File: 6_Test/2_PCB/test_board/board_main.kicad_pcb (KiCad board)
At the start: 4 copper layers, 100.5 x 75 mm, 80 parts, among them J1 PWR_Supply_Pins, J10 Chip_AVSS_GND_Jumpers, J11 Buffer_PWR_Jumper, J12 Reset_PWR_Jumpers, J13 Reset_Signal_Jumpers, J2 Analog_Input_Pins, J3 Digital_Input_Pins, J4 Digital_Output_Pins, J5 Chip_VDD_Jumpers, J6 BNC_Odd, J7 BNC_Even, J8 BNC_Jumpers, J9 Analog_Input_Jumpers, U1 TPS74501PDRVR, U2 ADA4807-1AKSZ-R7, U3 ADA4807-1AKSZ-R7, U4 TPS74501PDRVR, U5 SN74HC74DR, U6 CD4001BM96, U7 SN74LVC245APWR, U8 SN74LVC245APWR

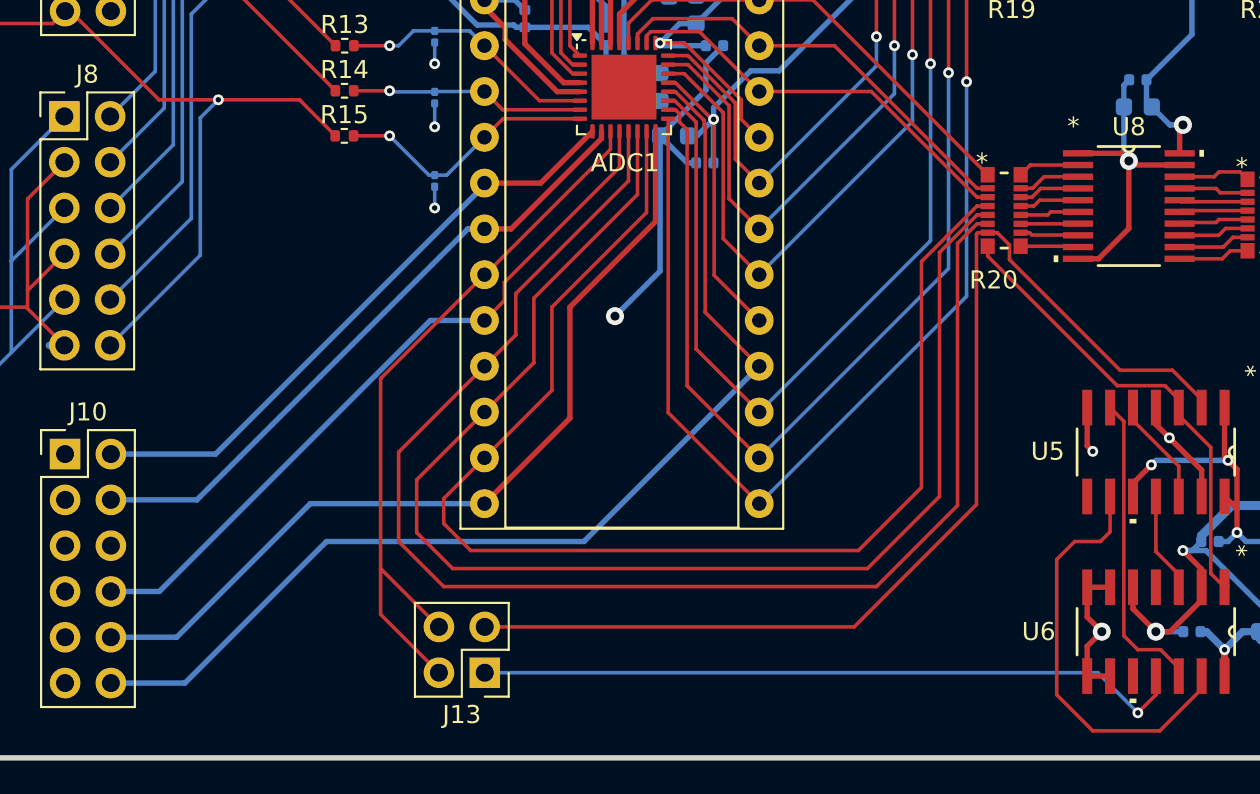
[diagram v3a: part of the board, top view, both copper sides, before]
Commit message: Fixed DRC errors
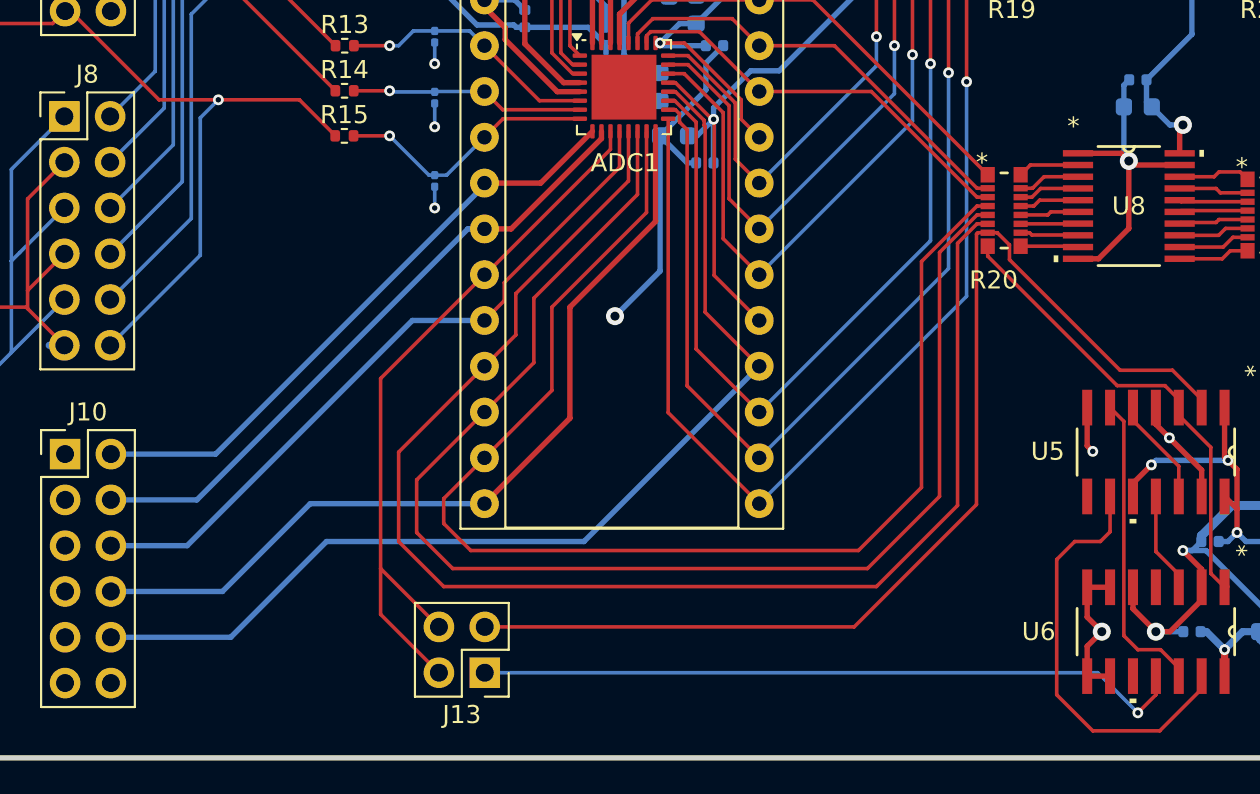
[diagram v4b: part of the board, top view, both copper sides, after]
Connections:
- J10 pad A3: /ADC/AVSS -> GND
- J10 pad B3: GND -> Net-(ADC1-IOVSS-Pad12)
- J10 pad B4: Net-(ADC1-IOVSS-Pad12) -> Net-(ADC1-VSS)
- J10 pad B5: Net-(ADC1-VSS) -> Net-(ADC1-IOVSS-Pad20)
- J10 pad B6: Net-(ADC1-IOVSS-Pad20) -> /ADC/AVSS
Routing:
- net Net-(ADC1-IOVSS-Pad12): track 40.5 -> 39.5 mm
- net Net-(ADC1-VSS): track 48.4 -> 47.3 mm
- net Net-(ADC1-IOVSS-Pad20): track 60.8 -> 59.7 mm
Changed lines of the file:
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@@
 		(tags "SN74LVC245APWR ")
 		(property "Reference" "U8"
-			(at 0 -4.3928 0)
+			(at 0 0 0)
 			(unlocked yes)
 			(layer "F.SilkS")
@@
 		(fp_text user "*"
 			(at -3.0734 -4.423601 0)
+			(unlocked yes)
+			(layer "F.SilkS")
+			(effects
+				(font
+					(size 1 1)
+					(thickness 0.15)
+				)
+			)
+		)
+		(fp_text user "*"
+			(at -3.0734 -4.423601 0)
 			(layer "F.SilkS")
 			(effects
@@
 		(fp_text user "*"
 			(at -3.0734 -4.423601 0)
+			(unlocked yes)
 			(layer "F.Fab")
 			(effects
@@
 		(fp_text user "*"
 			(at -3.0734 -4.423601 0)
-			(unlocked yes)
 			(layer "F.Fab")
 			(effects
@@
 			(pintype "power_in")
 		)
-		(model "${KIPRJMOD}/TestBoardEDA/SN74LVC245APWR.stp"
-			(offset
-				(xyz 0 0 0)
-			)
-			(scale
-				(xyz 1 1 1)
-			)
-			(rotate
-				(xyz 0 0 0)
-			)
-		)
 	)
 	(footprint "ECE628_lib:bnc_mini_gnd"
@@
 		)
 		(pad "A3" thru_hole oval
-			(at 2.54 5.08)
+			(at 0 5.08)
 			(size 1.7 1.7)
 			(drill 1)
 			(layers "*.Cu" "*.Mask")
 			(remove_unused_layers no)
-			(net 36 "/ADC/AVSS")
+			(net 34 "GND")
 			(pinfunction "A3")
 			(pintype "unspecified")
@@
 		)
 		(pad "B3" thru_hole oval
-			(at 0 5.08)
+			(at 2.54 5.08)
 			(size 1.7 1.7)
 			(drill 1)
 			(layers "*.Cu" "*.Mask")
 			(remove_unused_layers no)
-			(net 34 "GND")
+			(net 27 "Net-(ADC1-IOVSS-Pad12)")
 			(pinfunction "B3")
 			(pintype "unspecified")
@@
 			(layers "*.Cu" "*.Mask")
 			(remove_unused_layers no)
-			(net 27 "Net-(ADC1-IOVSS-Pad12)")
+			(net 6 "Net-(ADC1-VSS)")
 			(pinfunction "B4")
 			(pintype "unspecified")
@@
 			(layers "*.Cu" "*.Mask")
 			(remove_unused_layers no)
-			(net 6 "Net-(ADC1-VSS)")
+			(net 25 "Net-(ADC1-IOVSS-Pad20)")
 			(pinfunction "B5")
 			(pintype "unspecified")
@@
 			(layers "*.Cu" "*.Mask")
 			(remove_unused_layers no)
-			(net 25 "Net-(ADC1-IOVSS-Pad20)")
+			(net 36 "/ADC/AVSS")
 			(pinfunction "B6")
 			(pintype "unspecified")
@@
 	)
 	(segment
-		(start 97.19 132.81)
-		(end 93.54 132.81)
+		(start 93.54 130.27)
+		(end 99.73 130.27)
 		(width 0.3)
 		(layer "B.Cu")
@@
 	)
 	(segment
-		(start 104.6 125.4)
-		(end 97.19 132.81)
+		(start 99.73 130.27)
+		(end 104.6 125.4)
 		(width 0.3)
 		(layer "B.Cu")
@@
 	)
 	(segment
-		(start 93.54 135.35)
-		(end 97.65 135.35)
+		(start 100.19 132.81)
+		(end 93.54 132.81)
 		(width 0.3)
 		(layer "B.Cu")
@@
 	)
 	(segment
-		(start 119.78 127.5)
-		(end 129.5 117.78)
+		(start 105.5 127.5)
+		(end 100.19 132.81)
 		(width 0.3)
 		(layer "B.Cu")
@@
 	)
 	(segment
-		(start 97.65 135.35)
-		(end 105.5 127.5)
+		(start 119.78 127.5)
+		(end 129.5 117.78)
 		(width 0.3)
 		(layer "B.Cu")
@@
 	)
 	(segment
-		(start 93.54 130.27)
-		(end 96.23 130.27)
+		(start 93.54 127.73)
+		(end 97.77 127.73)
 		(width 0.3)
 		(layer "B.Cu")
@@
 	)
 	(segment
-		(start 111.26 115.24)
+		(start 110.26 115.24)
 		(end 114.26 115.24)
 		(width 0.3)
@@
 	)
 	(segment
-		(start 96.23 130.27)
-		(end 111.26 115.24)
+		(start 97.77 127.73)
+		(end 110.26 115.24)
 		(width 0.3)
 		(layer "B.Cu")

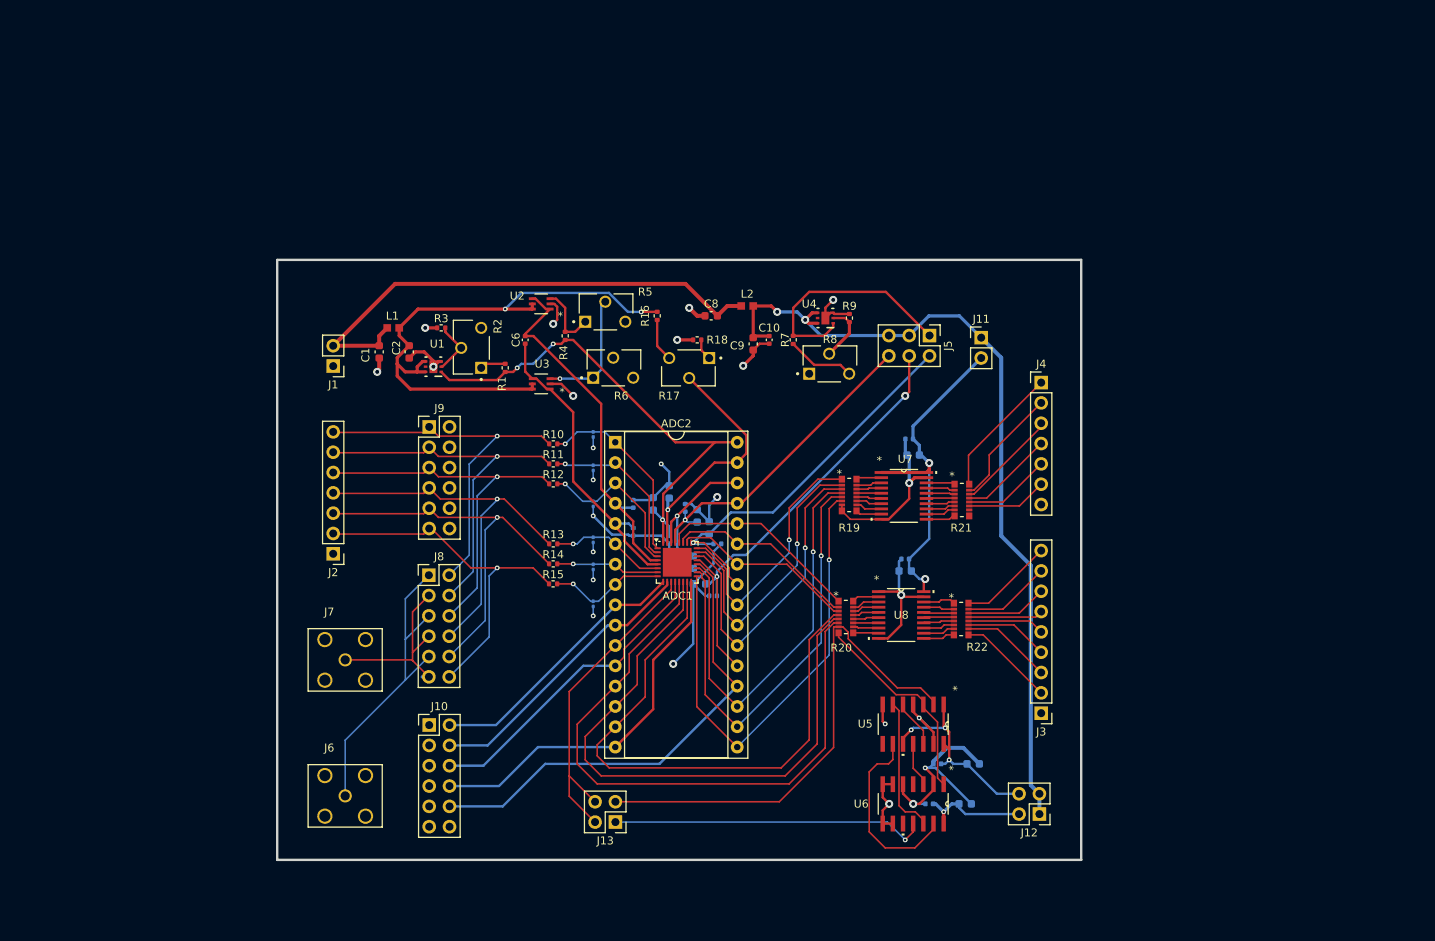
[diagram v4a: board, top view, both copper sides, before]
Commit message: Board Edits 250206
- Added the terminal block (4 positions - VSUP, GND, GND, & AVSS)
- Added vias for test points
- Added silkscreen labels for all inputs, jumpers, and potentiometers
- Widened traces going across the board
- Relabeled plane as AVSS plane
- Fixes to 3D model of board
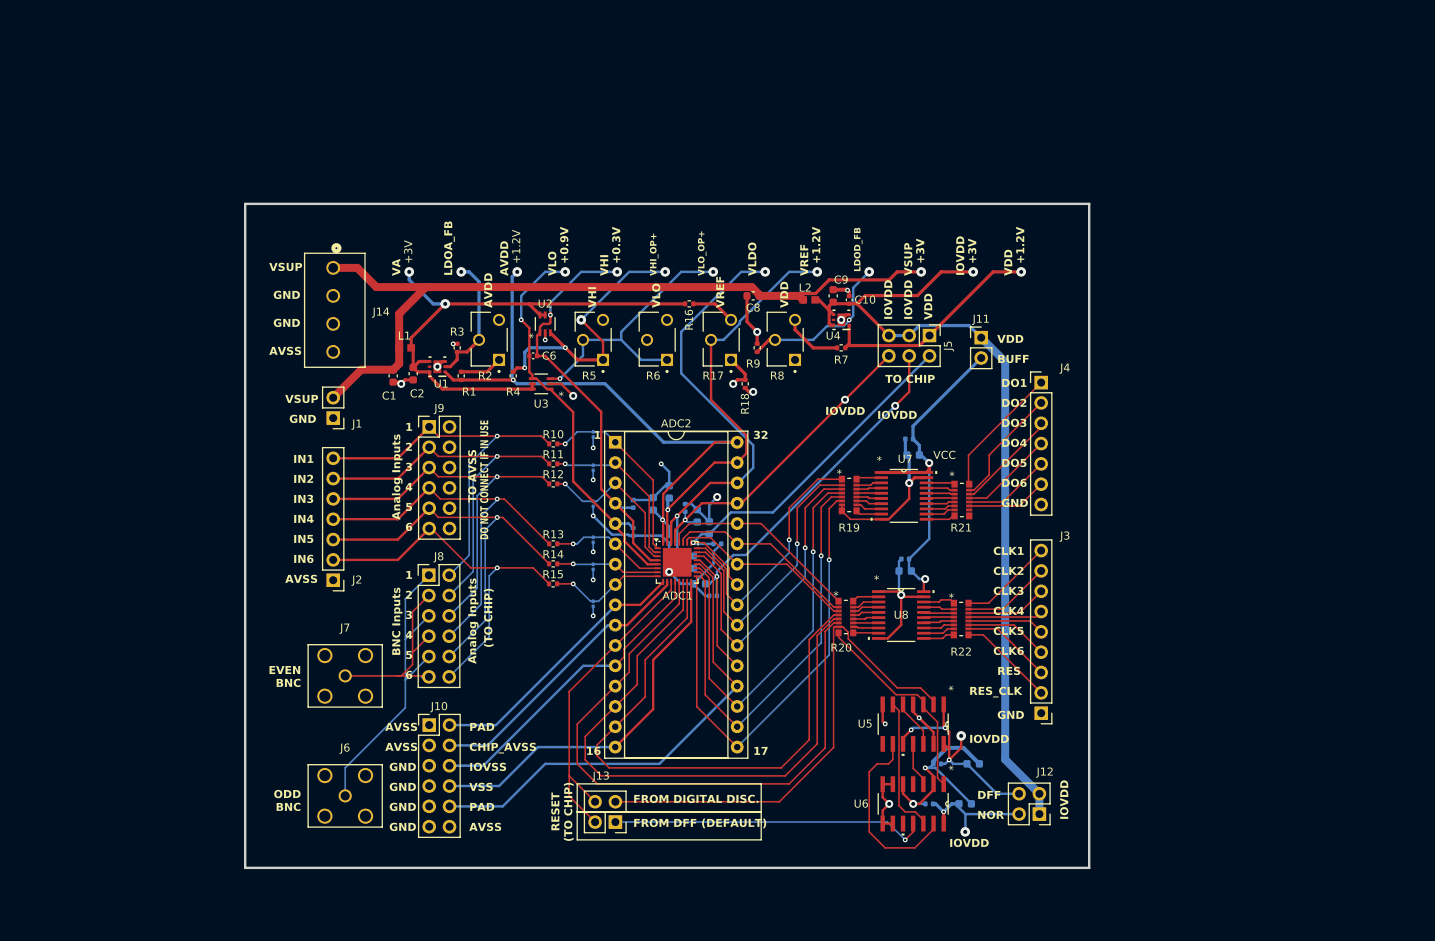
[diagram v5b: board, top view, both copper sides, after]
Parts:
- added J14: 1546551-4, TermBlck_4posFootprints:CONN4_1546551-4_TEC, F.Cu at (79.0, 65.5)
- moved R9 12.1 mm to (132.0, 75.5)
- moved C9 11.7 mm to (141.5, 69.0), turned to 90 degrees
- moved C10 11.2 mm to (143.5, 69.5), turned to 90 degrees
- moved R4 8.20 mm to (101.5, 79.0)
- moved R18 8.14 mm to (130.5, 80.0), turned to -90 degrees
- moved L2 7.79 mm to (138.5, 69.5)
- moved R6 6.52 mm to (119.5, 74.5), turned to 90 degrees
- moved J1 6.50 mm to (79.0, 84.3)
- moved R8 6.26 mm to (135.5, 74.5), turned to 90 degrees
- moved R7 6.08 mm to (142.5, 75.5), turned to 180 degrees
- moved C8 5.81 mm to (131.5, 69.0)
- moved R1 5.59 mm to (95.0, 79.0)
- moved R17 5.32 mm to (127.5, 74.5), turned to 90 degrees
- moved R16 4.27 mm to (123.5, 70.0), turned to 0 degrees
- moved R5 3.81 mm to (111.5, 74.5), turned to 90 degrees
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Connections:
- ADC1 pad 33: (no net) -> GND
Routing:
- net /ADC/VLDO: track 20.0 -> 57.1 mm, vias 1 -> 2
- net /AnalogSupply/VSUP: track 64.8 -> 98.4 mm, vias 0 -> 1
- net Net-(U2-+IN): track 8.39 -> 36.0 mm, vias 0 -> 4
- net /ADC/VREF: track 30.9 -> 51.5 mm, vias 1 -> 2
- net Net-(U3-+IN): track 15.6 -> 34.4 mm, vias 1 -> 2
- net GND: track 132.7 -> 117.8 mm
- net Net-(U4-FB): track 7.23 -> 20.3 mm, vias 0 -> 2
- net /ADC/VLO: track 38.2 -> 51.1 mm, vias 0 -> 2
- net /ADC/AVDD: track 64.1 -> 76.0 mm
- net Net-(U1-FB): track 6.80 -> 16.2 mm, vias 0 -> 1
- net /ADC/VHI: track 45.9 -> 53.1 mm, vias 0 -> 2
- net Net-(U5-*1CLR): track 34.2 -> 37.8 mm, vias 4 -> 5
- net /ADC/IN1: track 48.0 -> 50.4 mm
- net /ADC/IOVDD: track 104.4 -> 106.7 mm, vias 2 -> 1
- net Net-(R17-Pad1): track 2.68 -> 4.93 mm, vias 0 -> 1
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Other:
- board size 100.5 x 75 mm -> 105.5 x 83 mm
- board text added: "(TO CHIP)"
- board text added: "+0.3V"
- board text added: "+0.9V"
- board text added: "+1.2V"
- board text added: "+3V"
- board text added: "1"
- board text added: "16"
- board text added: "17"
- board text added: "2"
- board text added: "3"
- board text added: "32"
- board text added: "4"
- board text added: "5"
- board text added: "6"
- board text added: "AVDD"
- board text added: "AVSS"
- board text added: "Analog Inputs"
- board text added: "BNC Inputs"
- board text added: "BUFF"
- board text added: "CHIP_AVSS"
- board text added: "CLK1"
- board text added: "CLK2"
- board text added: "CLK3"
- board text added: "CLK4"
- board text added: "CLK5"
- board text added: "CLK6"
- board text added: "DFF"
- board text added: "DO NOT CONNECT IF IN USE"
- board text added: "DO1"
- board text added: "DO2"
- board text added: "DO3"
- board text added: "DO4"
- board text added: "DO5"
- board text added: "DO6"
- board text added: "EVEN BNC"
- board text added: "FROM DFF (DEFAULT)"
- board text added: "FROM DIGITAL DISC."
- board text added: "GND"
- board text added: "IN1"
- board text added: "IN2"
- board text added: "IN3"
- board text added: "IN4"
- board text added: "IN5"
- board text added: "IN6"
- board text added: "IOVDD"
- board text added: "IOVSS"
- board text added: "LDOA_FB"
- board text added: "LDOD_FB"
- board text added: "NOR"
- board text added: "ODD BNC"
- board text added: "PAD"
- board text added: "RES"
- board text added: "RESET (TO CHIP)"
- board text added: "RES_CLK"
- board text added: "TO AVSS"
- board text added: "TO CHIP"
- board text added: "VA"
- board text added: "VCC"
- board text added: "VDD"
- board text added: "VHI"
- board text added: "VHI_OP+"
- board text added: "VLDO"
- board text added: "VLO"
- board text added: "VLO_OP+"
- board text added: "VREF"
- board text added: "VSS"
- board text added: "VSUP"
